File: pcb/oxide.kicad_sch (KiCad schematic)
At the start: 121 parts, among them SW1 SW_MX, SW10 SW_MX, SW11 SW_MX, SW12 SW_MX, SW13 SW_MX, SW14 SW_MX, SW15 SW_MX, SW16 SW_MX, SW17 SW_MX, SW18 SW_MX, SW19 SW_MX, SW2 SW_MX, SW20 SW_MX, SW21 SW_MX, SW22 SW_MX, SW23 SW_MX, SW24 SW_MX, SW25 SW_MX, SW26 SW_MX, SW27 SW_MX, SW28 SW_MX, SW29 SW_MX, SW3 SW_MX, SW30 SW_MX, SW31 SW_MX, SW32 SW_MX, SW33 SW_MX, SW34 SW_MX, SW35 SW_MX, SW36 SW_MX, SW37 SW_MX, SW38 SW_MX, SW39 SW_MX, SW4 SW_MX, SW40 SW_MX, SW41 SW_MX, SW42 SW_MX, SW43 SW_MX, SW44 SW_MX, SW45 SW_MX, SW46 SW_MX, SW47 SW_MX, SW48 SW_MX, SW49 SW_MX, SW5 SW_MX, SW50 SW_MX, SW51 SW_MX, SW52 SW_MX, SW53 SW_MX, SW54 SW_MX, SW55 SW_MX, SW56 SW_MX, SW57 SW_MX, SW58 SW_MX, SW59 SW_MX, SW6 SW_MX, SW60 SW_MX, SW7 SW_MX, SW8 SW_MX, SW9 SW_MX

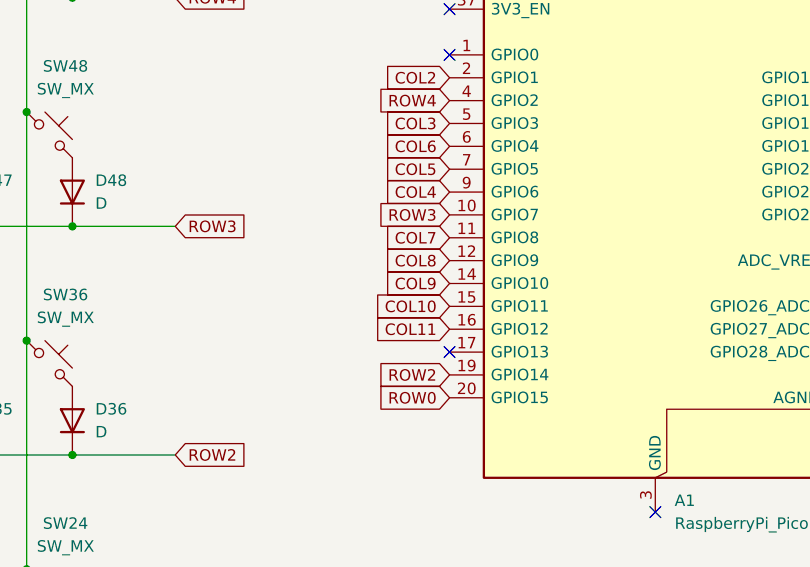
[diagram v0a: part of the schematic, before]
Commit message: Move Pico closer to the PCB edge and reroute traces
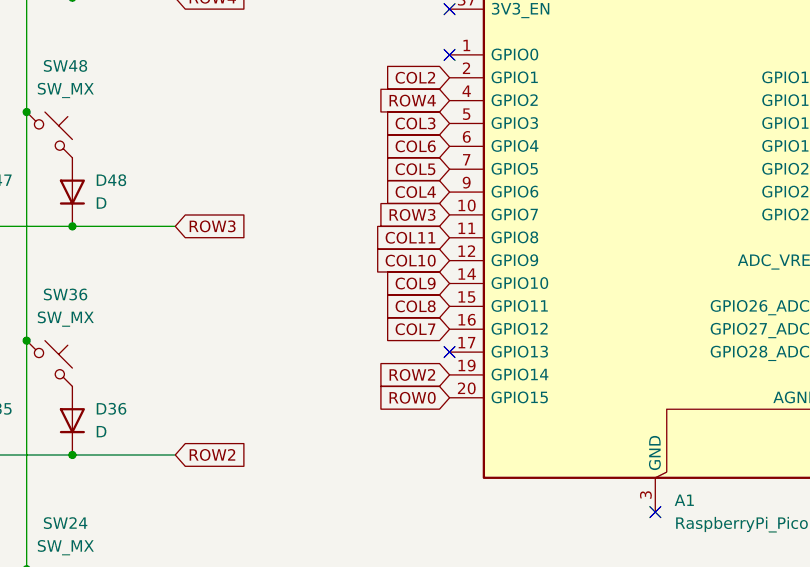
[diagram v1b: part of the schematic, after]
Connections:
- net COL10: now also A1.12 (GPIO9); no longer A1.15 (GPIO11)
- net COL11: now also A1.11 (GPIO8); no longer A1.16 (GPIO12)
- net COL7: now also A1.16 (GPIO12); no longer A1.11 (GPIO8)
- net COL8: now also A1.15 (GPIO11); no longer A1.12 (GPIO9)
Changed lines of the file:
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@@
 	(global_label "COL7"
 		(shape input)
-		(at 224.79 77.47 180)
+		(at 224.79 87.63 180)
 		(fields_autoplaced yes)
 		(effects
@@
 		)
 		(property "Intersheetrefs" "${INTERSHEET_REFS}"
-			(at 216.9667 77.47 0)
+			(at 216.9667 87.63 0)
 			(hide yes)
 			(show_name no)
@@
 	(global_label "COL11"
 		(shape input)
-		(at 224.79 87.63 180)
+		(at 224.79 77.47 180)
 		(fields_autoplaced yes)
 		(effects
@@
 		)
 		(property "Intersheetrefs" "${INTERSHEET_REFS}"
-			(at 215.7572 87.63 0)
+			(at 215.7572 77.47 0)
 			(hide yes)
 			(show_name no)
@@
 	(global_label "COL8"
 		(shape input)
-		(at 224.79 80.01 180)
+		(at 224.79 85.09 180)
 		(fields_autoplaced yes)
 		(effects
@@
 		)
 		(property "Intersheetrefs" "${INTERSHEET_REFS}"
-			(at 216.9667 80.01 0)
+			(at 216.9667 85.09 0)
 			(hide yes)
 			(show_name no)
@@
 	(global_label "COL10"
 		(shape input)
-		(at 224.79 85.09 180)
+		(at 224.79 80.01 180)
 		(fields_autoplaced yes)
 		(effects
@@
 		)
 		(property "Intersheetrefs" "${INTERSHEET_REFS}"
-			(at 215.7572 85.09 0)
+			(at 215.7572 80.01 0)
 			(hide yes)
 			(show_name no)
